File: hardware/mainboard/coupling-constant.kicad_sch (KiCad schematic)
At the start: 35 parts, among them J1 DC IN, J2 Input, J3 Output, U1 TC1044SxOA, U2 TL072

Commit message: hardware: fix mpn for resistor
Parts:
- R8: mpn RT0805FRE0720KL -> RT0805FRE074K7L
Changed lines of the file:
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@@
       (effects (font (size 1.27 1.27)) hide)
     )
-    (property "mpn" "RT0805FRE0720KL" (at 84.455 139.7 0)
+    (property "mpn" "RT0805FRE074K7L" (at 84.455 139.7 0)
       (effects (font (size 1.27 1.27)) hide)
     )

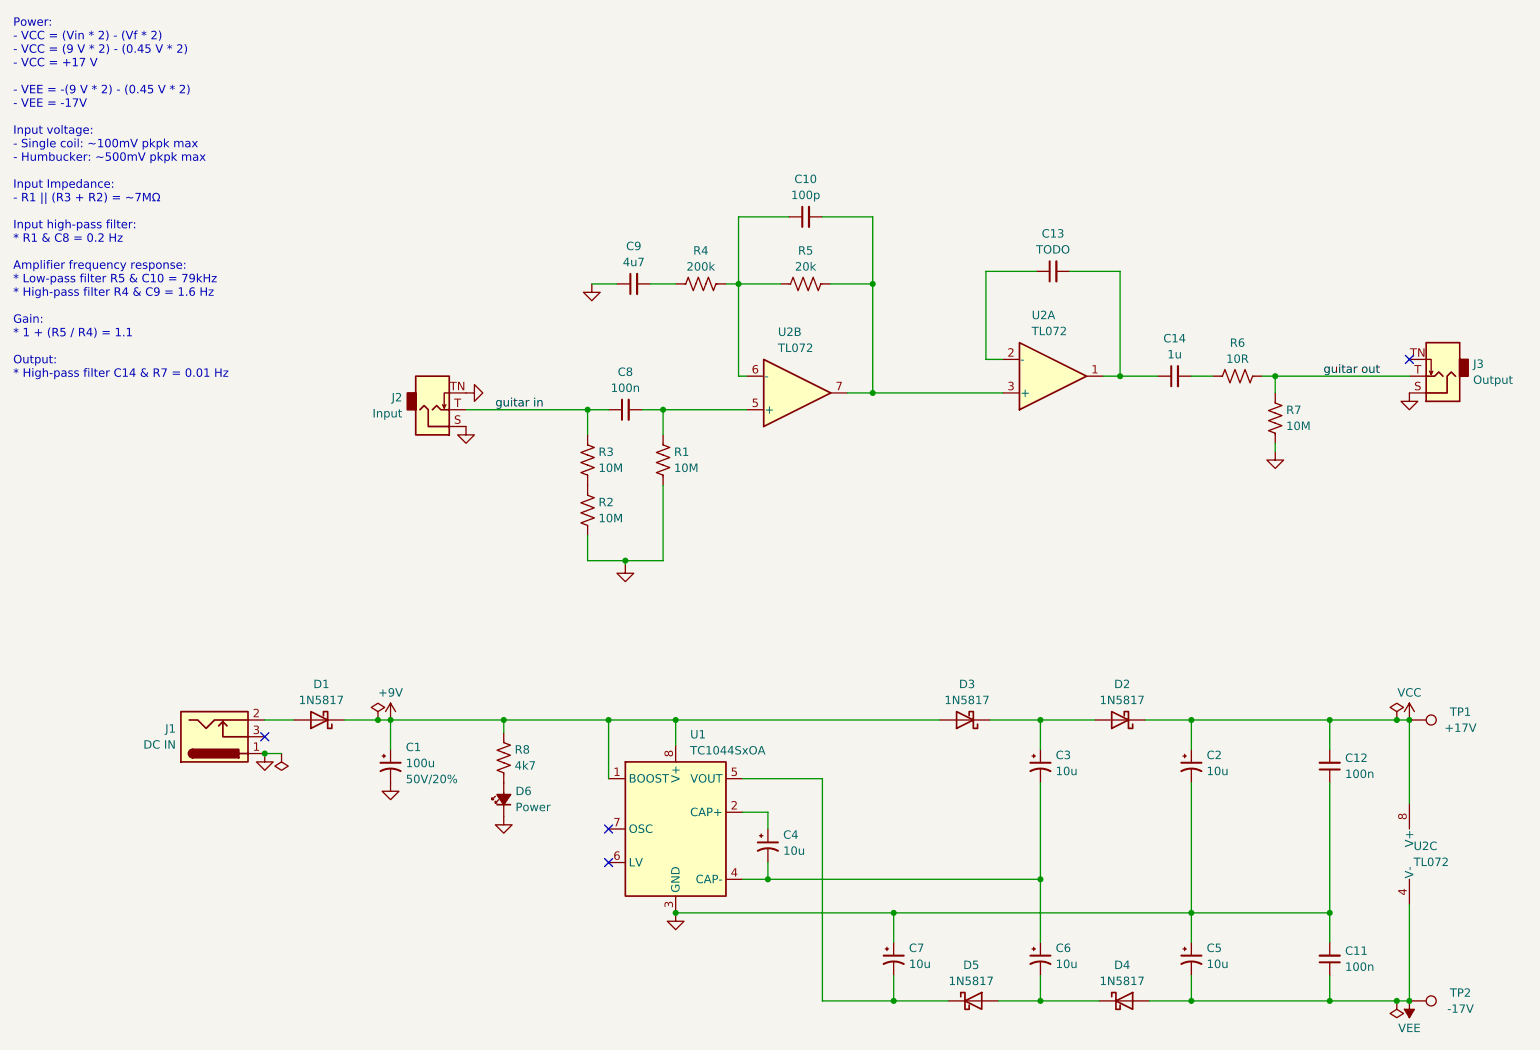
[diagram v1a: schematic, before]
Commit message: hardware: revision 2
- Swap TL072 for NJM2068
- Swap footprint for one compatible with SOIC-8 and DMP-8, making it easier to swap op-amps
- Remove feedback cap in output amplifier, it's not needed and has only caused problems.
- Update everything to KiCAD 8
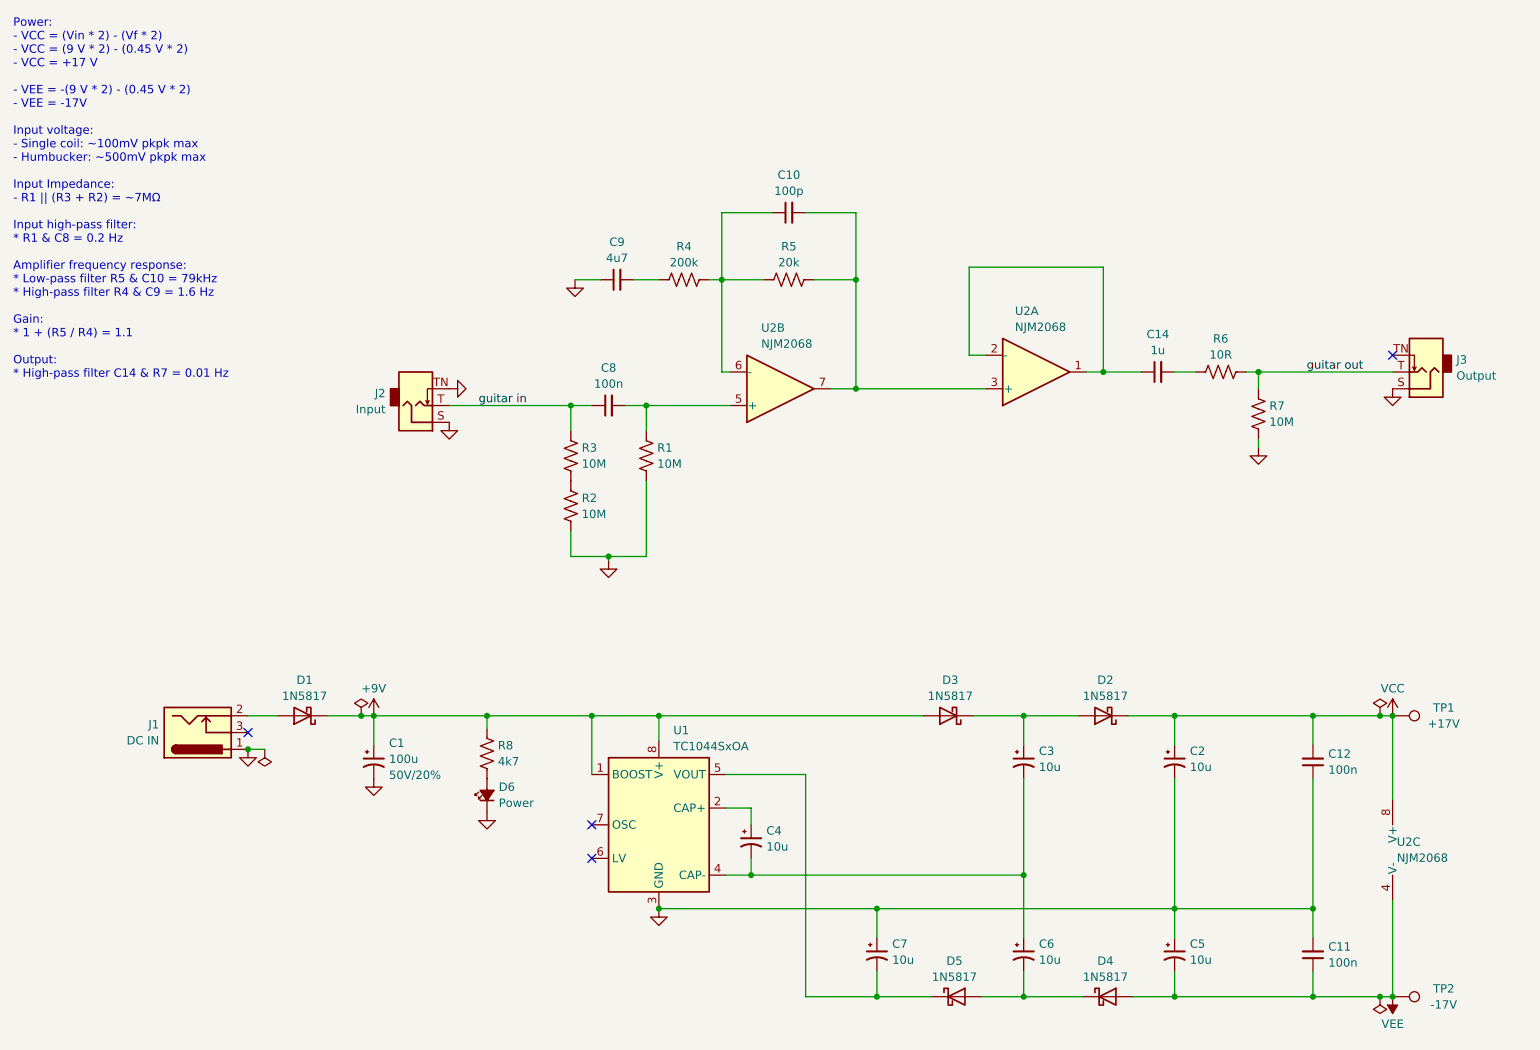
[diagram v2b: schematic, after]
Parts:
- removed C13: TODO, winterbloom:C_0805_HandSolder, symbol Device:C_Small
- U2: value TL072 -> NJM2068; footprint Package_SO:SOIC-8_3.9x4.9mm_P1.27mm -> winterbloom:SOIC-8+DMP-8_5mmx5mm_P1.27mm; Notes (none) -> Can substitute TL072 or TL072H; mpn (none) -> NJM2068M
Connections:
- net at U2.2 (-): now also C14.1, U2.1
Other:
- moved on the sheet: C1, C10, C11, C12, C14, C2, C3, C4, C5, C6, C7, C8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
